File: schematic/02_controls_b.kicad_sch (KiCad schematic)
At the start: 19 parts, among them SW107 F sharp, SW108 G, SW109 G sharp, SW110 A, SW111 A sharp, SW112 B, U402 74HC14

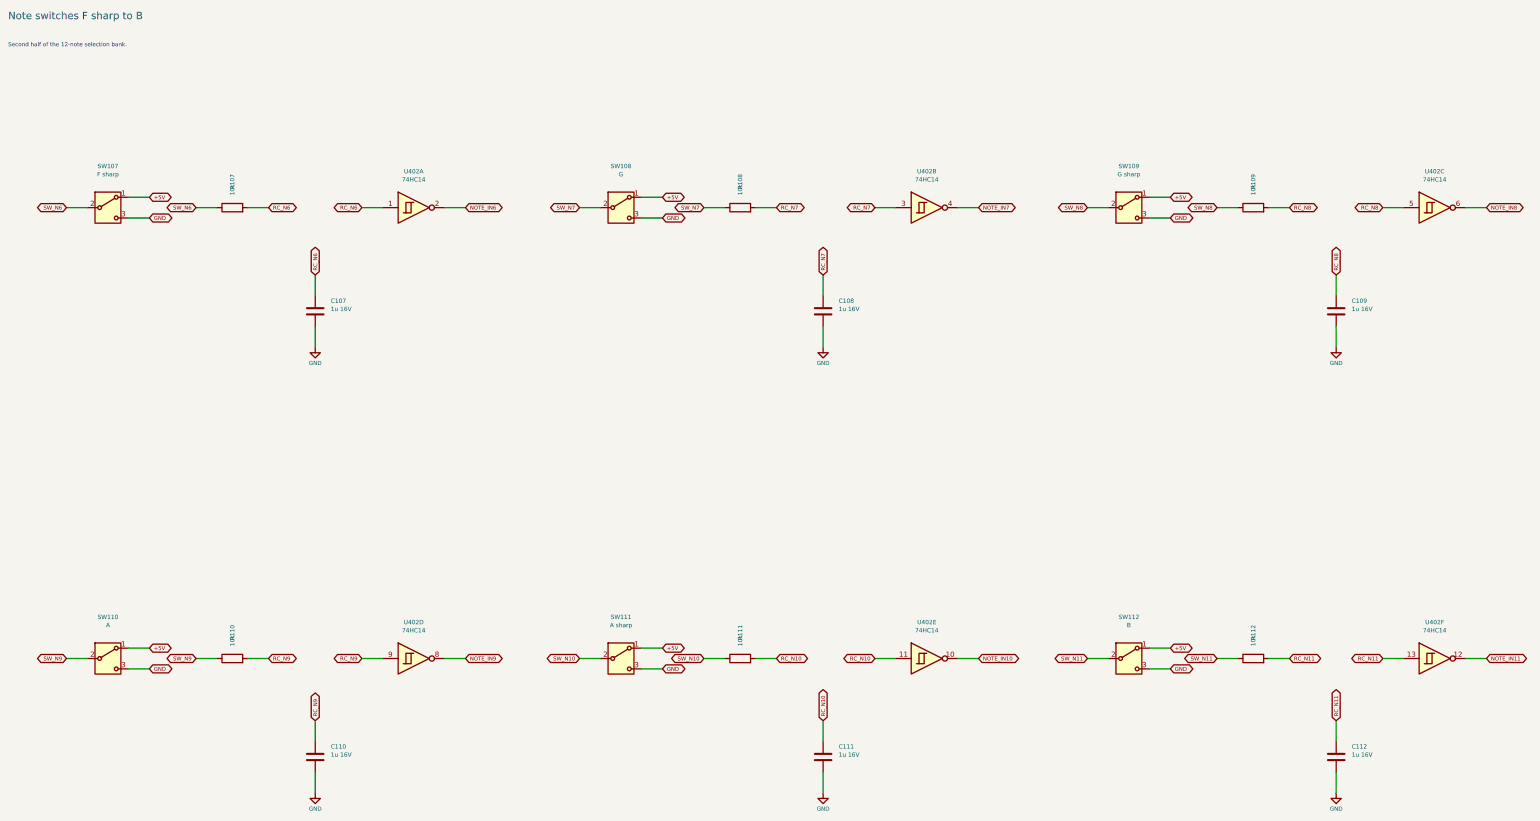
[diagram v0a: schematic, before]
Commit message: add the pitch and sound circuit
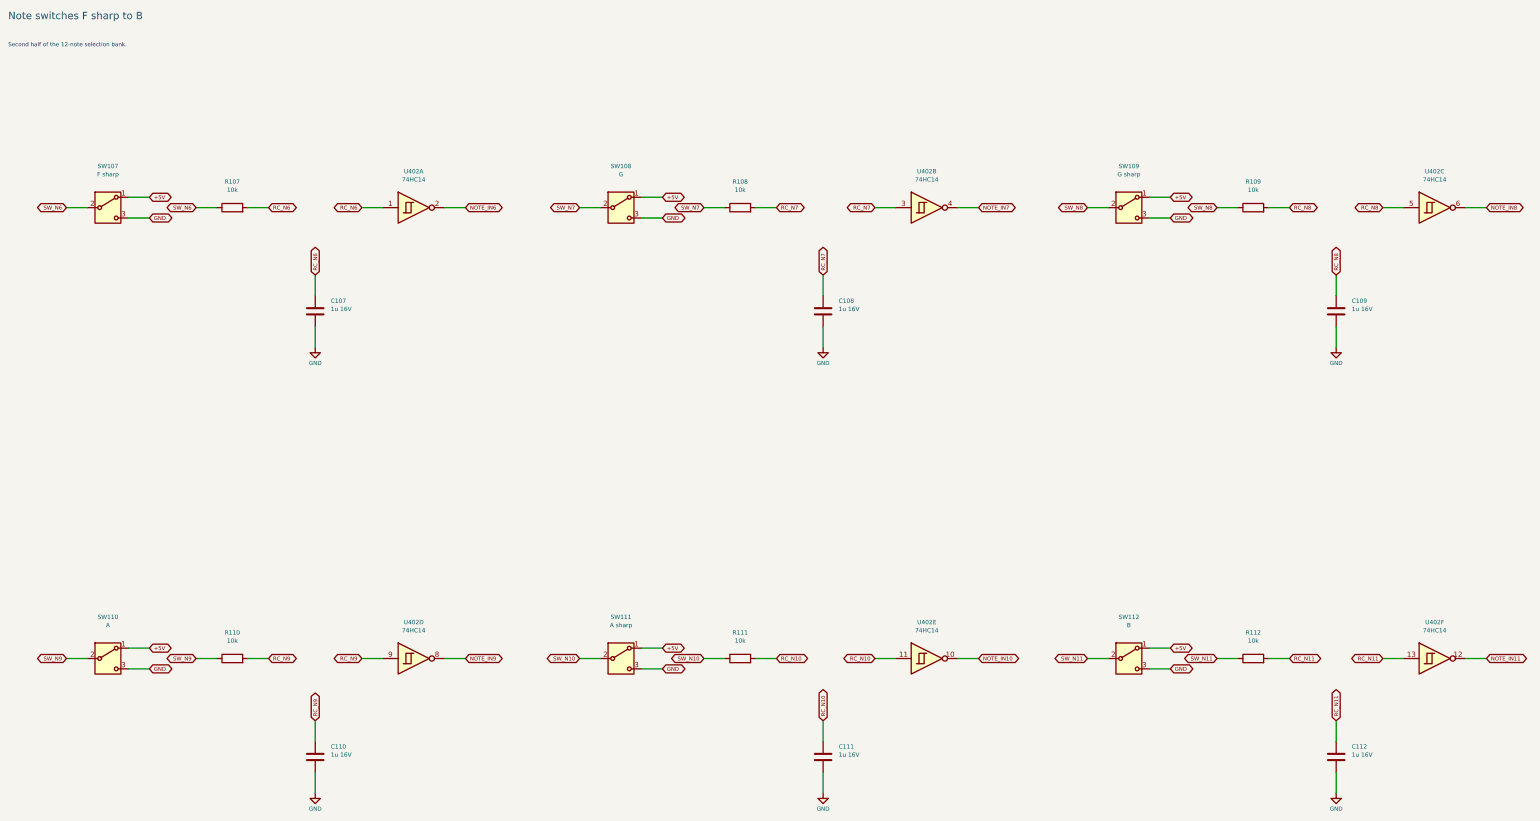
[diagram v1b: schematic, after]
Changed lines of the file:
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@@
     (dnp no)
     (property "Reference" "R107"
-      (at 74.93 58.419999999999995 0.0)
+      (at 74.93 58.419999999999995 90.0)
       (effects
         (font
@@
     )
     (property "Value" "10k"
-      (at 74.93 60.419999999999995 0.0)
+      (at 74.93 60.419999999999995 90.0)
       (effects
         (font
@@
     )
     (property "Footprint" "Resistor_SMD:R_0805_2012Metric"
-      (at 74.93 58.419999999999995 0.0)
+      (at 74.93 58.419999999999995 90.0)
       (effects
         (font
@@
     )
     (property "Datasheet" ""
-      (at 74.93 58.419999999999995 0.0)
+      (at 74.93 58.419999999999995 90.0)
       (effects
         (font
@@
     (dnp no)
     (property "Reference" "R108"
-      (at 199.39 58.419999999999995 0.0)
+      (at 199.39 58.419999999999995 90.0)
       (effects
         (font
@@
     )
     (property "Value" "10k"
-      (at 199.39 60.419999999999995 0.0)
+      (at 199.39 60.419999999999995 90.0)
       (effects
         (font
@@
     )
     (property "Footprint" "Resistor_SMD:R_0805_2012Metric"
-      (at 199.39 58.419999999999995 0.0)
+      (at 199.39 58.419999999999995 90.0)
       (effects
         (font
@@
     )
     (property "Datasheet" ""
-      (at 199.39 58.419999999999995 0.0)
+      (at 199.39 58.419999999999995 90.0)
       (effects
         (font
@@
     (dnp no)
     (property "Reference" "R109"
-      (at 325.12 58.419999999999995 0.0)
+      (at 325.12 58.419999999999995 90.0)
       (effects
         (font
@@
     )
     (property "Value" "10k"
-      (at 325.12 60.419999999999995 0.0)
+      (at 325.12 60.419999999999995 90.0)
       (effects
         (font
@@
     )
     (property "Footprint" "Resistor_SMD:R_0805_2012Metric"
-      (at 325.12 58.419999999999995 0.0)
+      (at 325.12 58.419999999999995 90.0)
       (effects
         (font
@@
     )
     (property "Datasheet" ""
-      (at 325.12 58.419999999999995 0.0)
+      (at 325.12 58.419999999999995 90.0)
       (effects
         (font
@@
     (dnp no)
     (property "Reference" "R110"
-      (at 74.93 168.91 0.0)
+      (at 74.93 168.91 90.0)
       (effects
         (font
@@
     )
     (property "Value" "10k"
-      (at 74.93 170.91 0.0)
+      (at 74.93 170.91 90.0)
       (effects
         (font
@@
     )
     (property "Footprint" "Resistor_SMD:R_0805_2012Metric"
-      (at 74.93 168.91 0.0)
+      (at 74.93 168.91 90.0)
       (effects
         (font
@@
     )
     (property "Datasheet" ""
-      (at 74.93 168.91 0.0)
+      (at 74.93 168.91 90.0)
       (effects
         (font
@@
     (dnp no)
     (property "Reference" "R111"
-      (at 199.39 168.91 0.0)
+      (at 199.39 168.91 90.0)
       (effects
         (font
@@
     )
     (property "Value" "10k"
-      (at 199.39 170.91 0.0)
+      (at 199.39 170.91 90.0)
       (effects
         (font
@@
     )
     (property "Footprint" "Resistor_SMD:R_0805_2012Metric"
-      (at 199.39 168.91 0.0)
+      (at 199.39 168.91 90.0)
       (effects
         (font
@@
     )
     (property "Datasheet" ""
-      (at 199.39 168.91 0.0)
+      (at 199.39 168.91 90.0)
       (effects
         (font
@@
     (dnp no)
     (property "Reference" "R112"
-      (at 325.12 168.91 0.0)
+      (at 325.12 168.91 90.0)
       (effects
         (font
@@
     )
     (property "Value" "10k"
-      (at 325.12 170.91 0.0)
+      (at 325.12 170.91 90.0)
       (effects
         (font
@@
     )
     (property "Footprint" "Resistor_SMD:R_0805_2012Metric"
-      (at 325.12 168.91 0.0)
+      (at 325.12 168.91 90.0)
       (effects
         (font
@@
     )
     (property "Datasheet" ""
-      (at 325.12 168.91 0.0)
-      (effects
-        (font
+      (at 325.12 168.91 90.0)
+      (effects
+        (font

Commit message: add power supply, rail checks and parts list
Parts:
- U402: MPN (none) -> 74HC14D,653; Manufacturer (none) -> Nexperia; Supplier (none) -> LCSC
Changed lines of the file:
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@@
       )
     )
-    (property "Datasheet" "http://www.ti.com/lit/gpn/sn74HC14"
+    (property "Datasheet" "https://assets.nexperia.com/documents/data-sheet/74HC_HCT14.pdf"
       (at 119.38 55.879999999999995 0.0)
       (effects
         (font
           (size 1.05 1.05)
+        )
+        (hide yes)
+      )
+    )
+    (property "MPN" "74HC14D,653"
+      (at 119.38 64.77 0.0)
+      (effects
+        (font
+          (size 1.0 1.0)
+        )
+        (hide yes)
+      )
+    )
+    (property "Manufacturer" "Nexperia"
+      (at 119.38 64.77 0.0)
+      (effects
+        (font
+          (size 1.0 1.0)
+        )
+        (hide yes)
+      )
+    )
+    (property "Supplier" "LCSC"
+      (at 119.38 64.77 0.0)
+      (effects
+        (font
+          (size 1.0 1.0)
         )
         (hide yes)
@@
       )
     )
-    (property "Datasheet" "http://www.ti.com/lit/gpn/sn74HC14"
+    (property "Datasheet" "https://assets.nexperia.com/documents/data-sheet/74HC_HCT14.pdf"
       (at 245.11 55.879999999999995 0.0)
       (effects
         (font
           (size 1.05 1.05)
+        )
+        (hide yes)
+      )
+    )
+    (property "MPN" "74HC14D,653"
+      (at 245.11 64.77 0.0)
+      (effects
+        (font
+          (size 1.0 1.0)
+        )
+        (hide yes)
+      )
+    )
+    (property "Manufacturer" "Nexperia"
+      (at 245.11 64.77 0.0)
+      (effects
+        (font
+          (size 1.0 1.0)
+        )
+        (hide yes)
+      )
+    )
+    (property "Supplier" "LCSC"
+      (at 245.11 64.77 0.0)
+      (effects
+        (font
+          (size 1.0 1.0)
         )
         (hide yes)
@@
       )
     )
-    (property "Datasheet" "http://www.ti.com/lit/gpn/sn74HC14"
+    (property "Datasheet" "https://assets.nexperia.com/documents/data-sheet/74HC_HCT14.pdf"
       (at 369.57 55.879999999999995 0.0)
       (effects
         (font
           (size 1.05 1.05)
+        )
+        (hide yes)
+      )
+    )
+    (property "MPN" "74HC14D,653"
+      (at 369.57 64.77 0.0)
+      (effects
+        (font
+          (size 1.0 1.0)
+        )
+        (hide yes)
+      )
+    )
+    (property "Manufacturer" "Nexperia"
+      (at 369.57 64.77 0.0)
+      (effects
+        (font
+          (size 1.0 1.0)
+        )
+        (hide yes)
+      )
+    )
+    (property "Supplier" "LCSC"
+      (at 369.57 64.77 0.0)
+      (effects
+        (font
+          (size 1.0 1.0)
         )
         (hide yes)
@@
       )
     )
-    (property "Datasheet" "http://www.ti.com/lit/gpn/sn74HC14"
+    (property "Datasheet" "https://assets.nexperia.com/documents/data-sheet/74HC_HCT14.pdf"
       (at 119.38 166.37 0.0)
       (effects
         (font
           (size 1.05 1.05)
+        )
+        (hide yes)
+      )
+    )
+    (property "MPN" "74HC14D,653"
+      (at 119.38 175.26 0.0)
+      (effects
+        (font
+          (size 1.0 1.0)
+        )
+        (hide yes)
+      )
+    )
+    (property "Manufacturer" "Nexperia"
+      (at 119.38 175.26 0.0)
+      (effects
+        (font
+          (size 1.0 1.0)
+        )
+        (hide yes)
+      )
+    )
+    (property "Supplier" "LCSC"
+      (at 119.38 175.26 0.0)
+      (effects
+        (font
+          (size 1.0 1.0)
         )
         (hide yes)
@@
       )
     )
-    (property "Datasheet" "http://www.ti.com/lit/gpn/sn74HC14"
+    (property "Datasheet" "https://assets.nexperia.com/documents/data-sheet/74HC_HCT14.pdf"
       (at 245.11 166.37 0.0)
       (effects
         (font
           (size 1.05 1.05)
+        )
+        (hide yes)
+      )
+    )
+    (property "MPN" "74HC14D,653"
+      (at 245.11 175.26 0.0)
+      (effects
+        (font
+          (size 1.0 1.0)
+        )
+        (hide yes)
+      )
+    )
+    (property "Manufacturer" "Nexperia"
+      (at 245.11 175.26 0.0)
+      (effects
+        (font
+          (size 1.0 1.0)
+        )
+        (hide yes)
+      )
+    )
+    (property "Supplier" "LCSC"
+      (at 245.11 175.26 0.0)
+      (effects
+        (font
+          (size 1.0 1.0)
         )
         (hide yes)
@@
       )
     )
-    (property "Datasheet" "http://www.ti.com/lit/gpn/sn74HC14"
+    (property "Datasheet" "https://assets.nexperia.com/documents/data-sheet/74HC_HCT14.pdf"
       (at 369.57 166.37 0.0)
       (effects
@@
         )
         (hide yes)
+      )
+    )
+    (property "MPN" "74HC14D,653"
+      (at 369.57 175.26 0.0)
+      (effects
+        (font
+          (size 1.0 1.0)
+        )
+        (hide yes)
+      )
+    )
+    (property "Manufacturer" "Nexperia"
+      (at 369.57 175.26 0.0)
+      (effects
+        (font
+          (size 1.0 1.0)
+        )
+        (hide yes)
+      )
+    )
+    (property "Supplier" "LCSC"
+      (at 369.57 175.26 0.0)
+      (effects
+        (font
+          (size 1.0 1.0)
+        )
+        (hide yes)
